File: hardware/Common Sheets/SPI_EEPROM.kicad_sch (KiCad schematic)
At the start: 3 parts, among them U4 M95320-RMN6

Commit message: Start on Digital IO card
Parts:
- C31: LibRef (none) -> ESD35C104K4T2A-24
- R26: LibRef (none) -> ERJ-3EKF33R0V
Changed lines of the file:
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@@
+			)
+		)
+		(property "LibRef" "ERJ-3EKF33R0V"
+			(at 111.76 77.47 90)
+			(effects
+				(font
+					(size 1.27 1.27)
+				)
+				(hide yes)
 			)
 		)
@@
 			(at 83.82 59.69 0)
 			(effects
+				(font
+					(size 1.27 1.27)
+				)
+				(hide yes)
+			)
+		)
+		(property "LibRef" "ESD35C104K4T2A-24"
+			(at 83.82 59.69 0)
+			(effects

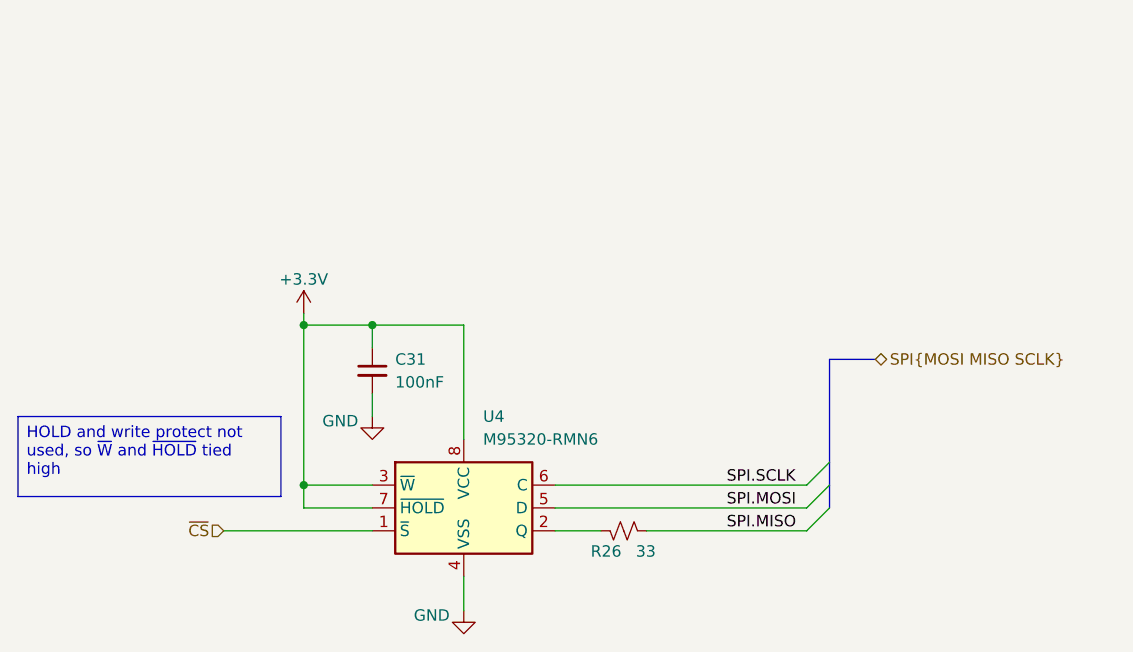
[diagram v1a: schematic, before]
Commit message: DIO card initial schematic done
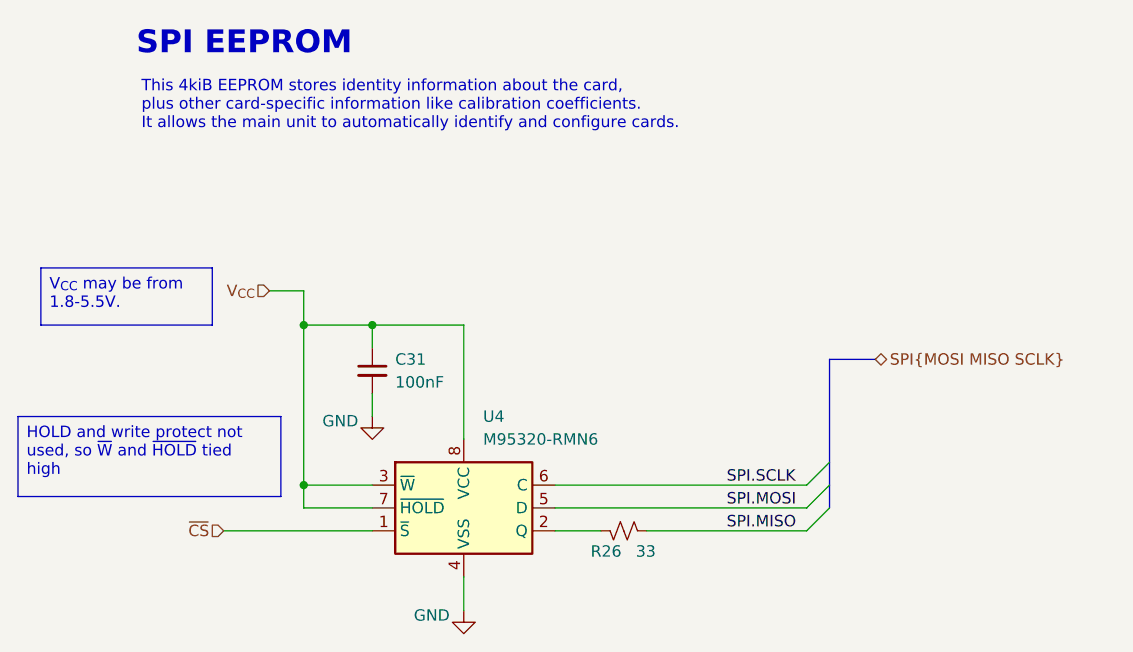
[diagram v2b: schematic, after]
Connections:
- net +3.3V renamed V_{CC}
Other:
- note added: "SPI EEPROM"
- note added: "This 4kiB EEPROM stores identity information about the card, plus other card-specific information like calibration coefficients. It allows the main unit to automatically identify and configure cards."
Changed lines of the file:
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@@
 		(title "SPI EEPROM")
+	)
+	(text "SPI EEPROM"
+		(exclude_from_sim no)
+		(at 69.596 23.368 0)
+		(effects
+			(font
+				(size 2.54 2.54)
+				(thickness 0.508)
+				(bold yes)
+			)
+		)
+	)
+	(text "This 4kiB EEPROM stores identity information about the card, \nplus other card-specific information like calibration coefficients.\nIt allows the main unit to automatically identify and configure cards."
+		(exclude_from_sim no)
+		(at 58.166 30.226 0)
+		(effects
+			(font
+				(size 1.27 1.27)
+			)
+			(justify left)
+		)
 	)
 	(text_box "HOLD and write protect not used, so ~{W} and ~{HOLD} tied high"
@@
 		)
 	)
+	(text_box "V_{CC} may be from 1.8-5.5V."
+		(exclude_from_sim no)
+		(at 46.99 48.26 0)
+		(size 19.05 6.35)
+		(margins 0.9525 0.9525 0.9525 0.9525)
+		(stroke
+			(width 0)
+			(type solid)
+		)
+		(fill
+			(type none)
+		)
+		(effects
+			(font
+				(size 1.27 1.27)
+			)
+			(justify left top)
+		)
+	)
 	(junction
 		(at 83.82 54.61)
@@
 	(wire
 		(pts
-			(xy 76.2 53.34) (xy 76.2 54.61)
+			(xy 76.2 50.8) (xy 76.2 54.61)
 		)
 		(stroke
@@
 		(pts
 			(xy 83.82 62.23) (xy 83.82 64.77)
+		)
+		(stroke
+			(width 0)
+			(type default)
+		)
+	)
+	(wire
+		(pts
+			(xy 76.2 50.8) (xy 72.39 50.8)
 		)
 		(stroke
@@
 			)
 			(justify left)
+		)
+	)
+	(hierarchical_label "V_{CC}"
+		(shape input)
+		(at 72.39 50.8 180)
+		(effects
+			(font
+				(size 1.27 1.27)
+			)
+			(justify right)
 		)
 	)
@@
 					(unit 1)
 				)
-			)
-		)
-	)
-	(symbol
-		(lib_id "power:+8V")
-		(at 76.2 53.34 0)
-		(unit 1)
-		(exclude_from_sim no)
-		(in_bom yes)
-		(on_board yes)
-		(dnp no)
-		(property "Reference" "#PWR048"
-			(at 76.2 57.15 0)
-			(effects
-				(font
-					(size 1.27 1.27)
-				)
-				(hide yes)
-			)
-		)
-		(property "Value" "+3.3V"
-			(at 76.2 49.53 0)
-			(effects
-				(font
-					(size 1.27 1.27)
-				)
-			)
-		)
-		(property "Footprint" ""
-			(at 76.2 53.34 0)
-			(effects
-				(font
-					(size 1.27 1.27)
-				)
-				(hide yes)
-			)
-		)
-		(property "Datasheet" ""
-			(at 76.2 53.34 0)
-			(effects
-				(font
-					(size 1.27 1.27)
-				)
-				(hide yes)
-			)
-		)
-		(property "Description" "Power symbol creates a global label with name \"+8V\""
-			(at 76.2 53.34 0)
-			(effects
-				(font
-					(size 1.27 1.27)
-				)
-				(hide yes)
-			)
-		)
-		(pin "1"
-		)
-		(instances
-			(project "HackerDAQ Voltage Card"
-				(path "/af2d881c-6553-449d-9093-6deb41497bdc/2388c7f7-4514-41da-b315-2dcc3aa57748"
-					(reference "#PWR048")
-					(unit 1)
-				)

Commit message: Finish redesigned DIO card
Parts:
- renumbered C31 to C5, R26 to R33, U4 to U9
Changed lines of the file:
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@@
 		(dnp no)
 		(fields_autoplaced yes)
-		(property "Reference" "U4"
+		(property "Reference" "U9"
 			(at 96.1233 64.77 0)
 			(effects
@@
 			(project ""
 				(path "/af2d881c-6553-449d-9093-6deb41497bdc/2388c7f7-4514-41da-b315-2dcc3aa57748"
-					(reference "U4")
+					(reference "U9")
 					(unit 1)
 				)
@@
 		(on_board yes)
 		(dnp no)
-		(property "Reference" "R26"
+		(property "Reference" "R33"
 			(at 111.506 79.756 90)
 			(effects
@@
 			(project "HackerDAQ Voltage Card"
 				(path "/af2d881c-6553-449d-9093-6deb41497bdc/2388c7f7-4514-41da-b315-2dcc3aa57748"
-					(reference "R26")
+					(reference "R33")
 					(unit 1)
 				)
@@
 		(dnp no)
 		(fields_autoplaced yes)
-		(property "Reference" "C31"
+		(property "Reference" "C5"
 			(at 86.36 58.4262 0)
 			(effects
@@
 			(project "HackerDAQ Voltage Card"
 				(path "/af2d881c-6553-449d-9093-6deb41497bdc/2388c7f7-4514-41da-b315-2dcc3aa57748"
-					(reference "C31")
+					(reference "C5")
 					(unit 1)
 				)

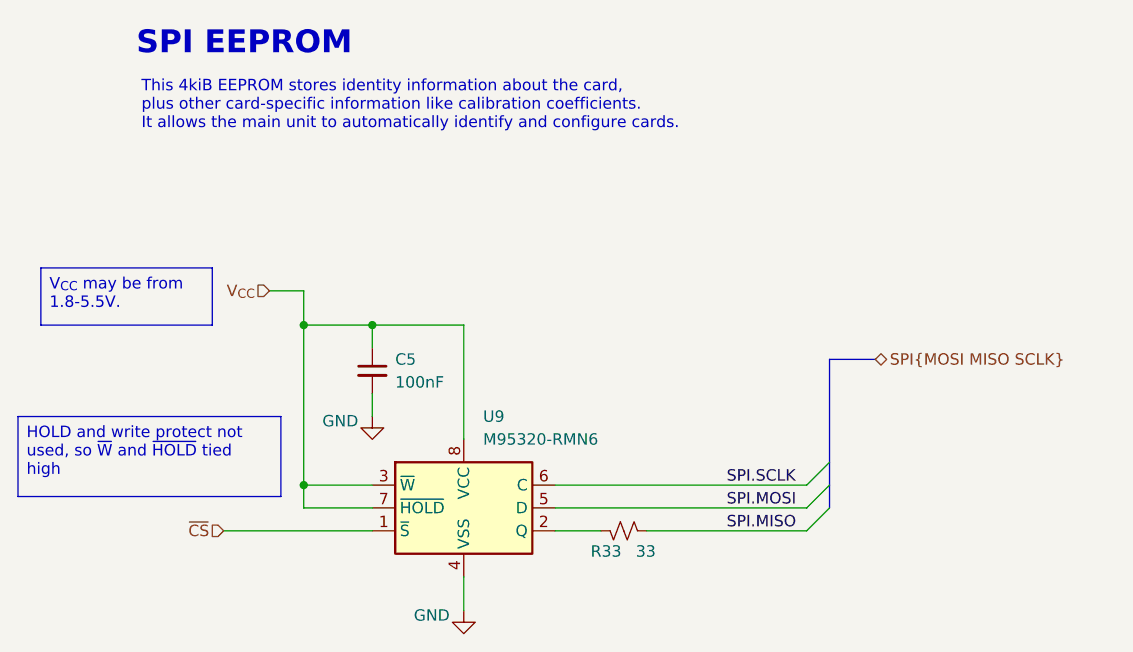
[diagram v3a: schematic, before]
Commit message: Route more of main unit, start on KiBot CI job
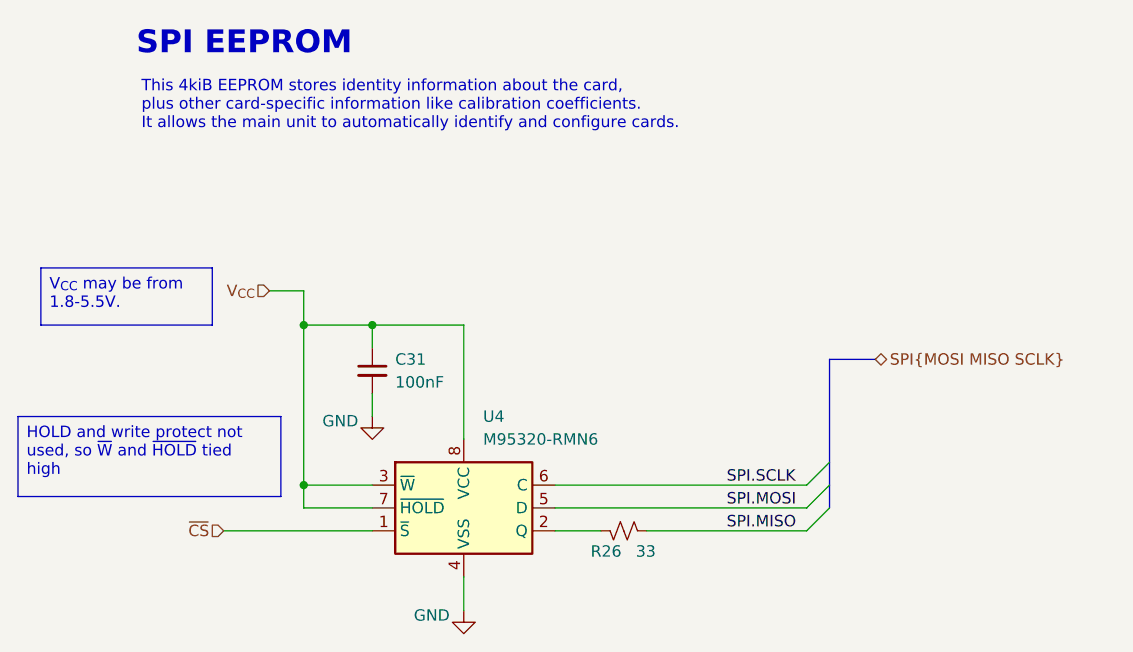
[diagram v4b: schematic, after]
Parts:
- renumbered C5 to C31, R33 to R26, U9 to U4
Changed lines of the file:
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@@
 		(dnp no)
 		(fields_autoplaced yes)
-		(property "Reference" "U9"
+		(property "Reference" "U4"
 			(at 96.1233 64.77 0)
 			(effects
@@
 			)
 		)
-		(property "Description" "SPI EEPROM, 4kiB (32kib), No Identification Page, 1.8 to 5.5V, SO8"
+		(property "Description" "SPI EEPROM, 256Kb (32K x 8), No Identification Page, 2.5 to 5.5V, SO8"
 			(at 93.98 74.93 0)
 			(effects
@@
 			(project ""
 				(path "/af2d881c-6553-449d-9093-6deb41497bdc/2388c7f7-4514-41da-b315-2dcc3aa57748"
-					(reference "U9")
+					(reference "U4")
 					(unit 1)
 				)
@@
 		(on_board yes)
 		(dnp no)
-		(property "Reference" "R33"
+		(property "Reference" "R26"
 			(at 111.506 79.756 90)
 			(effects
@@
 			)
 		)
-		(property "Description" "Resistor 33 ohm 1% 0.1W 0603"
+		(property "Description" "Resistor, small US symbol"
 			(at 111.76 77.47 0)
 			(effects
@@
 			(project "HackerDAQ Voltage Card"
 				(path "/af2d881c-6553-449d-9093-6deb41497bdc/2388c7f7-4514-41da-b315-2dcc3aa57748"
-					(reference "R33")
+					(reference "R26")
 					(unit 1)
 				)
@@
 		(dnp no)
 		(fields_autoplaced yes)
-		(property "Reference" "C5"
+		(property "Reference" "C31"
 			(at 86.36 58.4262 0)
 			(effects
@@
 			)
 		)
-		(property "Description" "Ceramic Cap 100nF +-10% 50V X7R 0603"
+		(property "Description" "Unpolarized capacitor, small symbol"
 			(at 83.82 59.69 0)
 			(effects
@@
 			(project "HackerDAQ Voltage Card"
 				(path "/af2d881c-6553-449d-9093-6deb41497bdc/2388c7f7-4514-41da-b315-2dcc3aa57748"
-					(reference "C5")
+					(reference "C31")
 					(unit 1)
 				)
